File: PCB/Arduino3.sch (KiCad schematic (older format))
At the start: 3 parts, among them U7 Arduino-Pro-5V

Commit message: Adding footprints cont.
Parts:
- H7: footprint (none) -> Footprints:Pin_Header_Straight_1x06_Pitch2.54mm
- U7: footprint (none) -> Footprints:ArduinoMINIPRO
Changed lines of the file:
@@
 F 0 "U7" H 4025 2100 60  0000 C CNN
 F 1 "Arduino-Pro-5V" H 4075 1950 60  0000 C CNN
-F 2 "" H 4875 2400 60  0001 C CNN
+F 2 "Footprints:ArduinoMINIPRO" H 4875 2400 60  0001 C CNN
 F 3 "" H 4875 2400 60  0001 C CNN
 	1    4575 2600
@@
 F 0 "H7" H 3800 1525 60  0000 C CNN
 F 1 "Header1" H 3900 1450 60  0001 C CNN
-F 2 "" H 3900 1425 60  0001 C CNN
+F 2 "Footprints:Pin_Header_Straight_1x06_Pitch2.54mm" H 3900 1425 60  0001 C CNN
 F 3 "" H 3900 1425 60  0001 C CNN
 	1    3900 1425

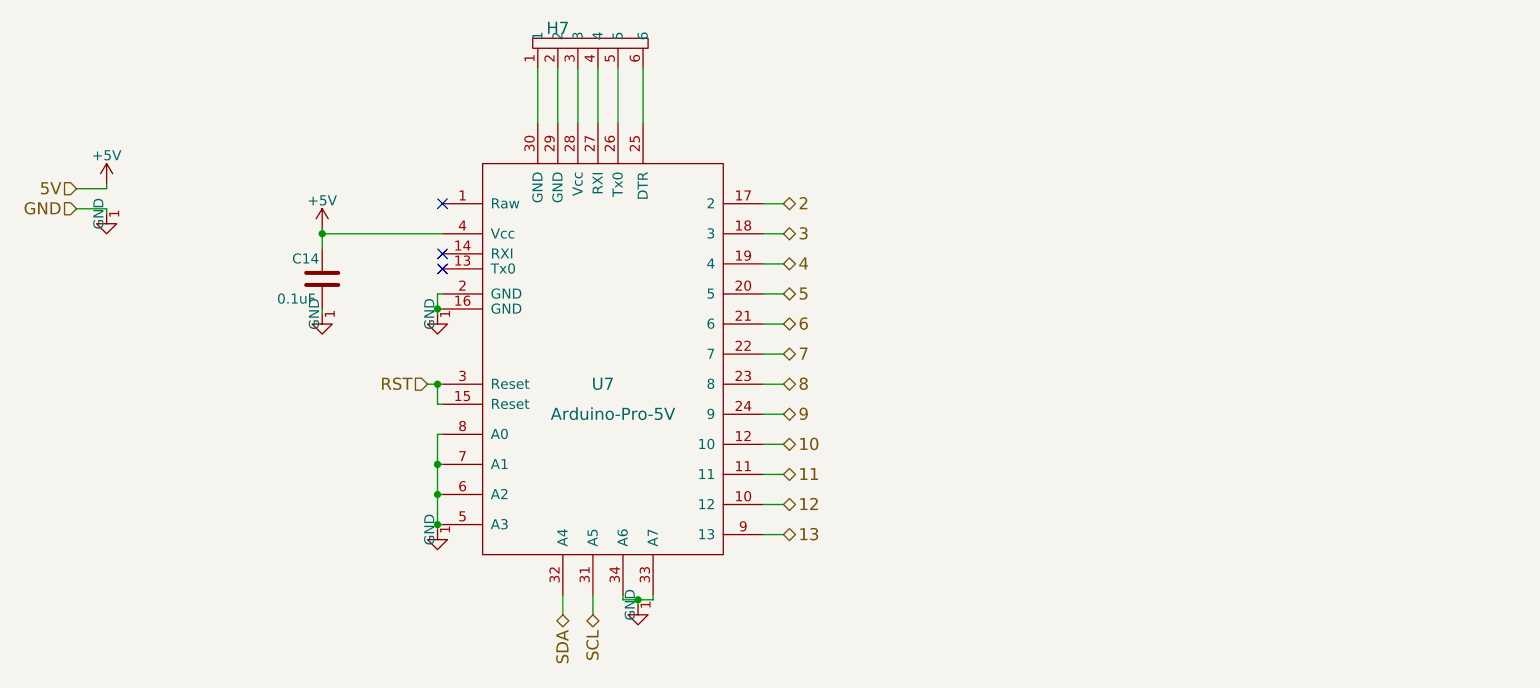
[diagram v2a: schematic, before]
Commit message: Added PCB layout
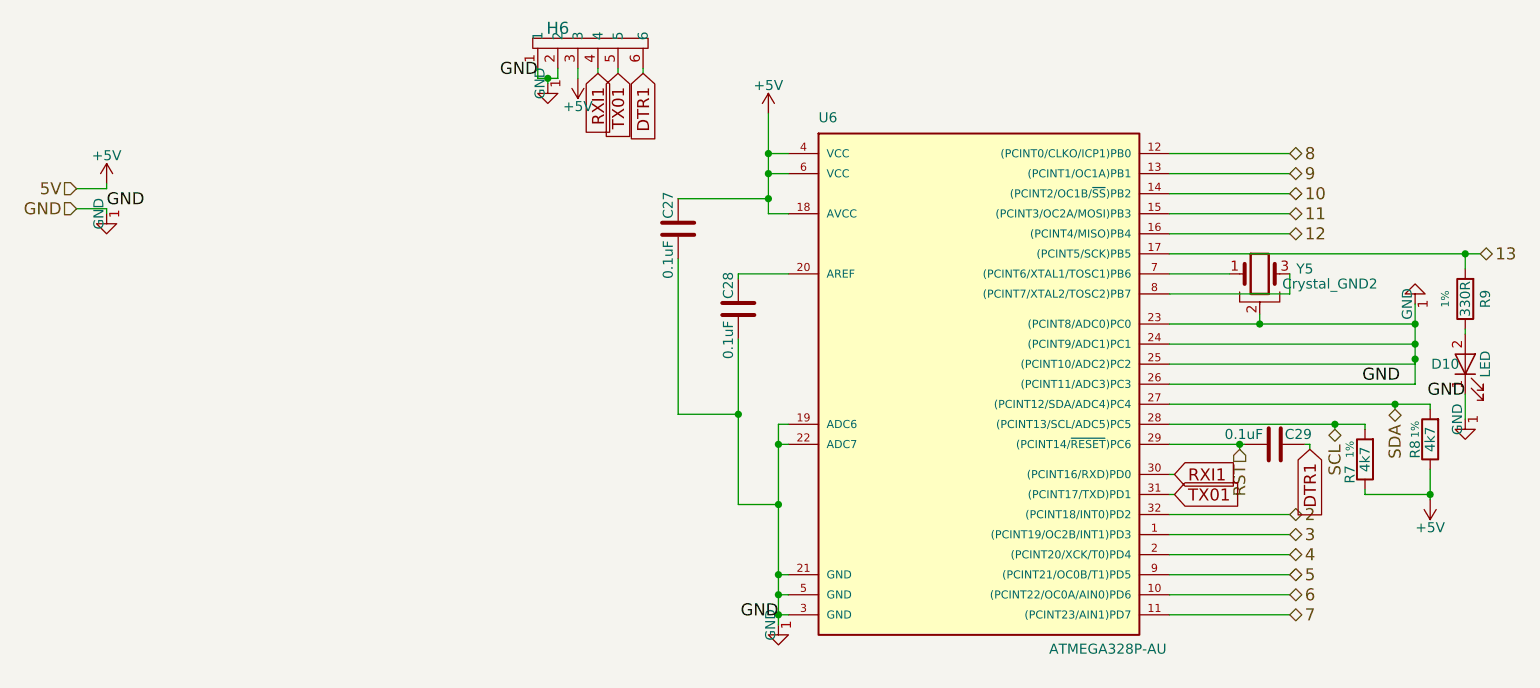
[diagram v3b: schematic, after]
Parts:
- removed C14: 0.1uF, symbol C
- removed U7: Arduino-Pro-5V, Footprints:ArduinoMINIPRO, symbol Arduino-Pro-5V
- added C27, C28, C29: 0.1uF, Capacitors_SMD:C_0603_HandSoldering, symbol C
- added D10: LED, LEDs:LED_0805_HandSoldering, symbol LED
- added R7, R8: 4k7, Resistors_SMD:R_0603_HandSoldering, symbol R
- added R9: 330R, Resistors_SMD:R_0603_HandSoldering, symbol R
- added U6: ATMEGA328P-AU, Housings_QFP:TQFP-32_7x7mm_Pitch0.8mm, symbol ATMEGA328P-AU
- added Y5: Crystal_GND2, Crystals:Resonator_SMD-3pin_7.2x3.0mm_HandSoldering, symbol Crystal_GND2
- H6: renamed from H7; footprint Footprints:Pin_Header_Straight_1x06_Pitch2.54mm -> Pin_Headers:Pin_Header_Straight_1x06_Pitch2.54mm
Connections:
- net +5V: now also H6.3, C27.1, R7.1, R8.1, U6.18 (AVCC), U6.4 (VCC), U6.6 (VCC)
- net 10: now also U6.14 ((PCINT2/OC1B/~SS~)PB2)
- net 11: now also U6.15 ((PCINT3/OC2A/MOSI)PB3)
- net 12: now also U6.16 ((PCINT4/MISO)PB4)
- net 13: now also R9.2, U6.17 ((PCINT5/SCK)PB5)
- net 2: now also U6.32 ((PCINT18/INT0)PD2)
- net 3: now also U6.1 ((PCINT19/OC2B/INT1)PD3)
- net 4: now also U6.2 ((PCINT20/XCK/T0)PD4)
- net 5: now also U6.9 ((PCINT21/OC0B/T1)PD5)
- net 6: now also U6.10 ((PCINT22/OC0A/AIN0)PD6)
- net 7: now also U6.11 ((PCINT23/AIN1)PD7)
- net 8: now also U6.12 ((PCINT0/CLKO/ICP1)PB0)
- net 9: now also U6.13 ((PCINT1/OC1A)PB1)
- net GND: now also H6.1, H6.2, C27.2, C28.2, D10.1 (K), U6.19 (ADC6), U6.21 (GND), U6.22 (ADC7), U6.23 ((PCINT8/ADC0)PC0), U6.24 ((PCINT9/ADC1)PC1), U6.25 ((PCINT10/ADC2)PC2), U6.26 ((PCINT11/ADC3)PC3), U6.3 (GND), U6.5 (GND), Y5.2
- net RST: now also C29.2, U6.29 ((PCINT14/~RESET~)PC6)
- net SCL: now also R7.2, U6.28 ((PCINT13/SCL/ADC5)PC5)
- net SDA: now also R8.2, U6.27 ((PCINT12/SDA/ADC4)PC4)
- net RXI1: now reaches H6.4
- net RXI1: now also U6.30 ((PCINT16/RXD)PD0)
- net TX01: now reaches H6.5
- net TX01: now also U6.31 ((PCINT17/TXD)PD1)
- net DTR1: now reaches H6.6
- net DTR1: now also C29.1
- new net: C28.1, U6.20 (AREF)
- new net: U6.7 ((PCINT6/XTAL1/TOSC1)PB6), Y5.1
- new net: U6.8 ((PCINT7/XTAL2/TOSC2)PB7), Y5.3
- new net: D10.2 (A), R9.1
- no-connect marks 3 -> 0

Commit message: PCB Done. To be reviewed.
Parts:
- removed D10: LED, LEDs:LED_0805_HandSoldering, symbol LED
- removed R9: 330R, Resistors_SMD:R_0603_HandSoldering, symbol R
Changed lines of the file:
@@
 GND
 $Comp
-L GND-RESCUE-Tardis #PWR50
+L GND-RESCUE-Tardis #PWR049
 U 1 1 5A31F3E8
 P 1550 2250
-F 0 "#PWR50" H 1550 2000 50  0001 C CNN
+F 0 "#PWR049" H 1550 2000 50  0001 C CNN
 F 1 "GND" H 1550 2100 50  0001 C CNN
 F 2 "" H 1550 2250 50  0001 C CNN
@@
 	1550 2225 1550 2250
 $Comp
-L +5V #PWR49
+L +5V #PWR050
 U 1 1 5A31F3F0
 P 1550 2100
-F 0 "#PWR49" H 1550 1950 50  0001 C CNN
+F 0 "#PWR050" H 1550 1950 50  0001 C CNN
 F 1 "+5V" H 1550 2240 50  0000 C CNN
 F 2 "" H 1550 2100 50  0001 C CNN
@@
 	6850 2450 8400 2450
 $Comp
-L R R9
-U 1 1 5A52FC60
-P 8325 2675
-F 0 "R9" V 8225 2675 50  0000 C CNN
-F 1 "330R" V 8325 2675 50  0000 C CNN
-F 2 "Resistors_SMD:R_0603_HandSoldering" V 8255 2675 50  0001 C CNN
-F 3 "" H 8325 2675 50  0001 C CNN
-F 4 "1%" V 8425 2675 39  0000 C CNN "%"
-	1    8325 2675
-	-1   0    0    1
-$EndComp
-$Comp
-L LED D10
-U 1 1 5A532C18
-P 8325 3000
-F 0 "D10" V 8325 3100 50  0000 C CNN
-F 1 "LED" H 8325 2900 50  0000 C CNN
-F 2 "LEDs:LED_0805_HandSoldering" H 8325 3000 50  0001 C CNN
-F 3 "" H 8325 3000 50  0001 C CNN
-	1    8325 3000
-	0    -1   -1   0
-$EndComp
-Text Label 8325 3175 2    60   ~ 0
-GND
-Wire Wire Line
-	8325 2825 8325 2850
-Wire Wire Line
-	8325 2525 8325 2450
-Connection ~ 8325 2450
-Wire Wire Line
-	8325 3150 8325 3275
-$Comp
-L GND-RESCUE-Tardis #PWR57
-U 1 1 5A532DD4
-P 8325 3275
-F 0 "#PWR57" H 8325 3025 50  0001 C CNN
-F 1 "GND" H 8325 3125 50  0001 C CNN
-F 2 "" H 8325 3275 50  0001 C CNN
-F 3 "" H 8325 3275 50  0001 C CNN
-	1    8325 3275
-	1    0    0    -1
-$EndComp
-$Comp
-L GND-RESCUE-Tardis #PWR55
+L GND-RESCUE-Tardis #PWR051
 U 1 1 5A535047
 P 8075 2700
-F 0 "#PWR55" H 8075 2450 50  0001 C CNN
+F 0 "#PWR051" H 8075 2450 50  0001 C CNN
 F 1 "GND" H 8075 2550 50  0001 C CNN
 F 2 "" H 8075 2700 50  0001 C CNN
@@
 $EndComp
 $Comp
-L +5V #PWR56
+L +5V #PWR052
 U 1 1 5A535804
 P 8150 3675
-F 0 "#PWR56" H 8150 3525 50  0001 C CNN
+F 0 "#PWR052" H 8150 3525 50  0001 C CNN
 F 1 "+5V" H 8150 3815 50  0000 C CNN
 F 2 "" H 8150 3675 50  0001 C CNN
@@
 Connection ~ 8150 3650
 $Comp
-L +5V #PWR52
+L +5V #PWR053
 U 1 1 5A536837
 P 3900 1575
-F 0 "#PWR52" H 3900 1425 50  0001 C CNN
+F 0 "#PWR053" H 3900 1425 50  0001 C CNN
 F 1 "+5V" H 3900 1715 50  0000 C CNN
 F 2 "" H 3900 1575 50  0001 C CNN
@@
 	4225 1525 4225 1550
 $Comp
-L GND-RESCUE-Tardis #PWR51
+L GND-RESCUE-Tardis #PWR054
 U 1 1 5A536BFF
 P 3750 1600
-F 0 "#PWR51" H 3750 1350 50  0001 C CNN
+F 0 "#PWR054" H 3750 1350 50  0001 C CNN
 F 1 "GND" H 3750 1450 50  0001 C CNN
 F 2 "" H 3750 1600 50  0001 C CNN
@@
 Connection ~ 7200 3400
 $Comp
-L GND-RESCUE-Tardis #PWR54
+L GND-RESCUE-Tardis #PWR055
 U 1 1 5A53805F
 P 4900 4300
-F 0 "#PWR54" H 4900 4050 50  0001 C CNN
+F 0 "#PWR055" H 4900 4050 50  0001 C CNN
 F 1 "GND" H 4900 4150 50  0001 C CNN
 F 2 "" H 4900 4300 50  0001 C CNN
@@
 Connection ~ 4900 3700
 $Comp
-L +5V #PWR53
+L +5V #PWR056
 U 1 1 5A5386E7
 P 4850 1750
-F 0 "#PWR53" H 4850 1600 50  0001 C CNN
+F 0 "#PWR056" H 4850 1600 50  0001 C CNN
 F 1 "+5V" H 4850 1890 50  0000 C CNN
 F 2 "" H 4850 1750 50  0001 C CNN
